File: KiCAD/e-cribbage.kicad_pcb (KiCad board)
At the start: 2 copper layers, 304.8 x 100.3 mm, 569 parts, among them J1 Conn_01x04_Female, U1 74HC595D_118, U10 74HC595D_118, U11 74HC595D_118, U12 74HC595D_118, U13 74HC595D_118, U14 74HC595D_118, U15 74HC595D_118, U16 74HC595D_118, U17 74HC595D_118, U18 74HC595D_118, U19 74HC595D_118, U2 MSP430F2012IPW, U20 74HC595D_118, U21 74HC595D_118, U22 74HC595D_118, U23 74HC595D_118, U24 74HC595D_118, U25 74HC595D_118, U26 74HC595D_118, U27 74HC595D_118, U28 74HC595D_118, U29 74HC595D_118, U3 74HC595D_118, U30 74HC595D_118, U31 74HC595D_118, U32 SN74LVC1G08DBVR, U34 SN74LVC1G08DBVR, U35 SN74LVC1G08DBVR, U36 SN74LVC1G08DBVR, U37 SN74LVC1G08DBVR, U38 SN74LVC1G08DBVR, U39 SN74LVC1G08DBVR, U4 74HC595D_118, U40 SN74LVC1G08DBVR, U5 74HC595D_118, U6 74HC595D_118, U7 74HC595D_118, U8 74HC595D_118, U9 74HC595D_118

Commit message: initial routing complete
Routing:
- net CLK2B: track 114.2 -> 430.7 mm, vias 4 -> 8
- net CLK1B: track 281.6 -> 478.3 mm, vias 1 -> 5
- net Net-(U13-Pad9): track 0.00 -> 143.7 mm, vias 0 -> 6
- net CLK1C: track 44.0 -> 176.4 mm, vias 2 -> 4
- net CLK2C: track 244.9 -> 375.6 mm, vias 2 -> 5
- net CLK2A: track 325.9 -> 436.0 mm, vias 4 -> 7
- net Net-(U11-Pad9): track 0.00 -> 102.4 mm, vias 0 -> 2
- net Net-(U27-Pad9): track 0.00 -> 90.5 mm, vias 0 -> 2
- net Net-(U22-Pad9): track 0.00 -> 73.7 mm, vias 0 -> 2
- net Net-(U10-Pad14): track 0.00 -> 69.2 mm, vias 0 -> 2
- net Net-(U8-Pad9): track 0.00 -> 66.4 mm, vias 0 -> 2
- net Net-(U24-Pad9): track 0.00 -> 65.6 mm, vias 0 -> 2
- net Net-(U10-Pad9): track 0.00 -> 46.1 mm, vias 0 -> 4
- net Net-(U6-Pad9): track 0.00 -> 42.8 mm, vias 0 -> 3
- net Net-(U28-Pad9): track 0.00 -> 42.2 mm, vias 0 -> 2
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
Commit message: Layout - routed switch, usb, linear reg
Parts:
- added J2: USB_B_Micro, Connector_USB:USB_Micro-B_Molex_47346-0001, F.Cu at (58.5, 177.8)
- added S5: EG1218, digikey-footprints:Switch_Slide_11.6x4mm_EG1218, F.Cu at (73.5, 174.8)
- added U33: TPS22929D, Package_TO_SOT_SMD:SOT-23-6, F.Cu at (73.3, 168.8)
- added U41: LM317T, digikey-footprints:TO-220-3, F.Cu at (67.2, 168.1)
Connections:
- BAT1 pad 1: +3V3 -> +BATT
- C2 pad 1: +3V3 -> VS
- J1 pad 1: +3V3 -> VS
- R243 pad 2: +3V3 -> VS
- R244 pad 2: +3V3 -> VS
- R246 pad 2: +3V3 -> VS
- R247 pad 2: +3V3 -> VS
- R251 pad 2: +3V3 -> VS
- U16 pad 9: (no net) -> Net-(U16-Pad9)
- U2 pad 1: +3V3 -> VS
- U2 pad 6: (no net) -> Net-(U2-Pad6)
- U2 pad 9: (no net) -> Net-(U2-Pad9)
- U23 pad 9: (no net) -> Net-(U23-Pad9)
- U24 pad 14: (no net) -> Net-(U24-Pad14)
- U31 pad 9: (no net) -> Net-(U31-Pad9)
- U7 pad 9: (no net) -> Net-(U7-Pad9)
- U8 pad 14: (no net) -> Net-(U8-Pad14)
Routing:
- net VS: track 0.00 -> 132.3 mm, vias 0 -> 8
- net Net-(U2-Pad9): track 0.00 -> 91.0 mm, vias 0 -> 4
- net GND: track 949.0 -> 1034.0 mm, vias 335 -> 336
- net +BATT: track 0.00 -> 31.3 mm
- net +3V3: track 498.9 -> 483.5 mm, vias 90 -> 88
- net Net-(J2-Pad1): track 0.00 -> 10.4 mm, vias 0 -> 1
- net Net-(S5-Pad3): track 0.00 -> 9.19 mm
- net DATA: track 202.4 -> 208.1 mm
- net Net-(C33-Pad1): track 212.3 -> 208.1 mm
- net Net-(C32-Pad1): track 187.8 -> 183.9 mm
- net Net-(C35-Pad1): track 188.6 -> 185.0 mm
- net Net-(C34-Pad1): track 173.3 -> 170.2 mm
- net LE1: track 74.3 -> 75.4 mm

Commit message: Layout: routed USB power and switch, silkscreen
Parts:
- added C40: 1.0uF, Capacitor_SMD:C_0603_1608Metric_Pad1.05x0.95mm_HandSolder, F.Cu at (89.2, 171.7)
- added C41: 1.0uF, Capacitor_SMD:C_0603_1608Metric_Pad1.05x0.95mm_HandSolder, F.Cu at (81.7, 171.3)
- added C42: 1.0uF, Capacitor_SMD:C_0603_1608Metric_Pad1.05x0.95mm_HandSolder, F.Cu at (55.6, 171.1)
- added C43: 1.0uF, Capacitor_SMD:C_0603_1608Metric_Pad1.05x0.95mm_HandSolder, F.Cu at (64.1, 172.3)
- C4: footprint Capacitors_SMD:C_0603_HandSoldering -> Capacitor_SMD:C_0603_1608Metric_Pad1.05x0.95mm_HandSolder
- S5: footprint digikey-footprints:Switch_Slide_11.6x4mm_EG1218 -> Button_Switch_SMD:SW_SPDT_CK-JS102011SAQN
- U41: value LM317T -> TLV71333PDBV; footprint digikey-footprints:TO-220-3 -> Package_TO_SOT_SMD:SOT-23-5
- moved U33 12.8 mm to (85.9, 171.4)
- moved U41 6.94 mm to (60.8, 170.9), turned to 0 degrees
- moved S5 3.70 mm to (70.5, 176.9), turned to 0 degrees
- moved C18 0.89 mm to (206.3, 90.2)
- moved J2 0.51 mm to (58.5, 177.3)
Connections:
- J2 pad 1: Net-(J2-Pad1) -> Net-(C42-Pad1)
- S5 pad 1: +BATT -> Net-(C43-Pad1)
- S5 pad 3: Net-(S5-Pad3) -> +BATT
- U1 pad 12: CLK1A -> RCLK
- U10 pad 12: CLK1C -> RCLK
- U11 pad 12: CLK1C -> RCLK
- U12 pad 12: CLK1C -> RCLK
- U13 pad 12: CLK1C -> RCLK
- U14 pad 12: CLK1D -> RCLK
- U15 pad 12: CLK1D -> RCLK
- U16 pad 12: CLK1D -> RCLK
- U17 pad 12: CLK2A -> RCLK
- U18 pad 12: CLK2A -> RCLK
- U19 pad 12: CLK2A -> RCLK
- U2 pad 6: Net-(U2-Pad6) -> RCLK
- U20 pad 12: CLK2A -> RCLK
- U21 pad 12: CLK2B -> RCLK
- U22 pad 12: CLK2B -> RCLK
- U23 pad 12: CLK2B -> RCLK
- U24 pad 12: CLK2B -> RCLK
- U25 pad 12: CLK2C -> RCLK
- U26 pad 12: CLK2C -> RCLK
- U27 pad 12: CLK2C -> RCLK
- U28 pad 12: CLK2C -> RCLK
- U29 pad 12: CLK2D -> RCLK
- U3 pad 12: CLK1A -> RCLK
- U30 pad 12: CLK2D -> RCLK
- U31 pad 12: CLK2D -> RCLK
- U4 pad 12: CLK1A -> RCLK
- U41 pad 1: GND -> Net-(C42-Pad1)
- U41 pad 2: Net-(S5-Pad3) -> GND
- U41 pad 3: Net-(J2-Pad1) -> Net-(C42-Pad1)
- U5 pad 12: CLK1A -> RCLK
- U6 pad 12: CLK1B -> RCLK
- U7 pad 12: CLK1B -> RCLK
- U8 pad 12: CLK1B -> RCLK
- U8 pad 14: Net-(U8-Pad14) -> Net-(U7-Pad9)
- U9 pad 12: CLK1B -> RCLK
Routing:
- net RCLK: track 0.00 -> 768.1 mm, vias 0 -> 12
- net CLK2A: track 436.0 -> 325.4 mm, vias 7 -> 4
- net CLK1A: track 378.9 -> 314.4 mm, vias 6 -> 5
- net GND: track 1034.0 -> 1002.9 mm, vias 336 -> 349
- net +3V3: track 483.5 -> 464.1 mm, vias 88 -> 90
- net Net-(C42-Pad1): track 0.00 -> 14.0 mm
- net Net-(C43-Pad1): track 0.00 -> 10.7 mm
- net Net-(J2-Pad1): track 10.4 -> 0.00 mm, vias 1 -> 0
- net CLK1B: track 478.3 -> 468.5 mm, vias 5 -> 4
- net Net-(S5-Pad3): track 9.19 -> 0.00 mm
- net Net-(C34-Pad1): track 170.2 -> 163.2 mm
- net Net-(C33-Pad1): track 208.1 -> 201.2 mm
- net Net-(C32-Pad1): track 183.9 -> 177.0 mm
- net Net-(C35-Pad1): track 185.0 -> 178.1 mm
- net Net-(U2-Pad9): track 91.0 -> 85.3 mm, vias 4 -> 6
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
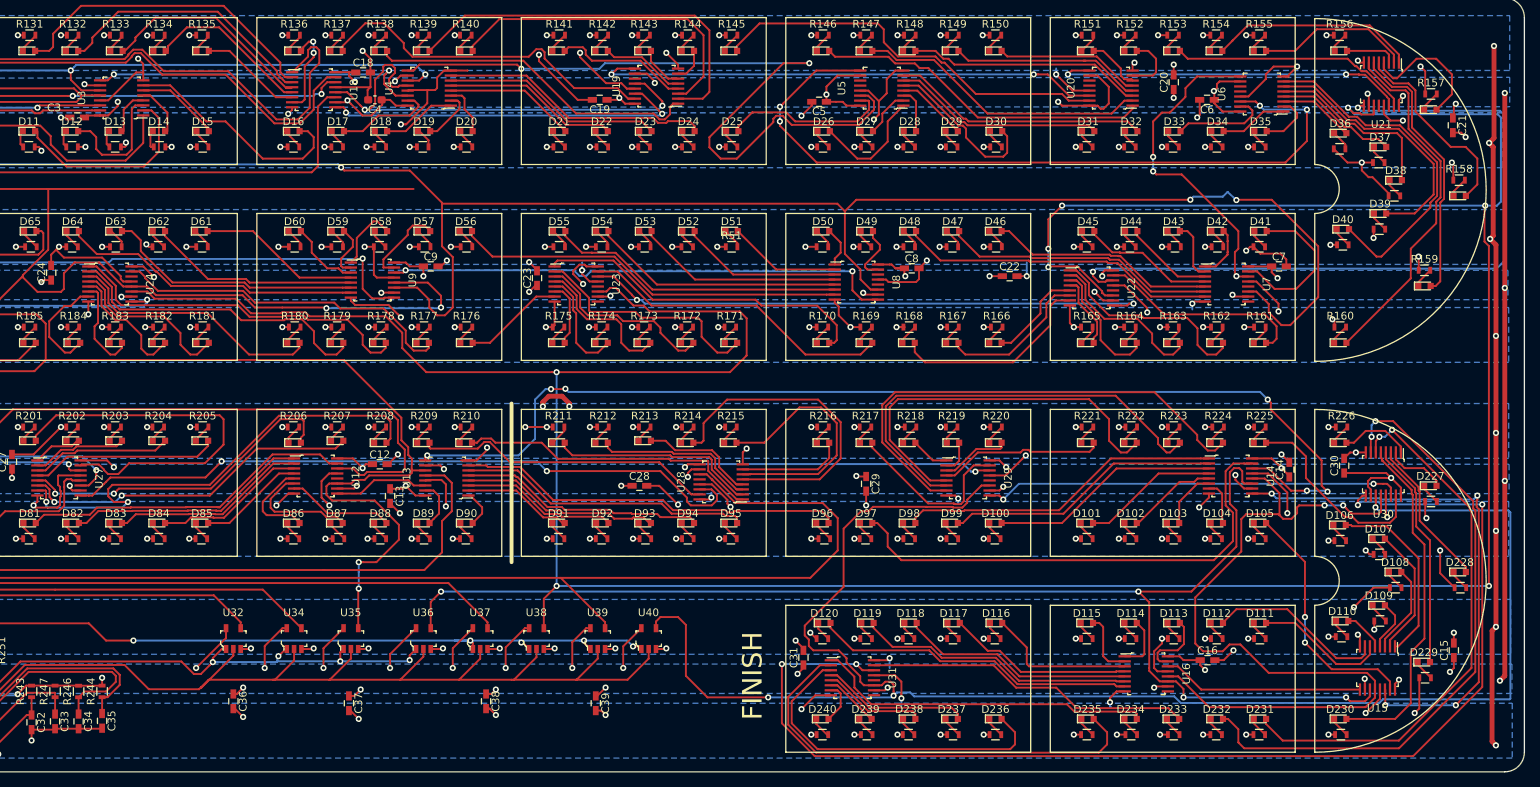
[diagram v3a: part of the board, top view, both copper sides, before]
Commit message: Finished RCLK routes
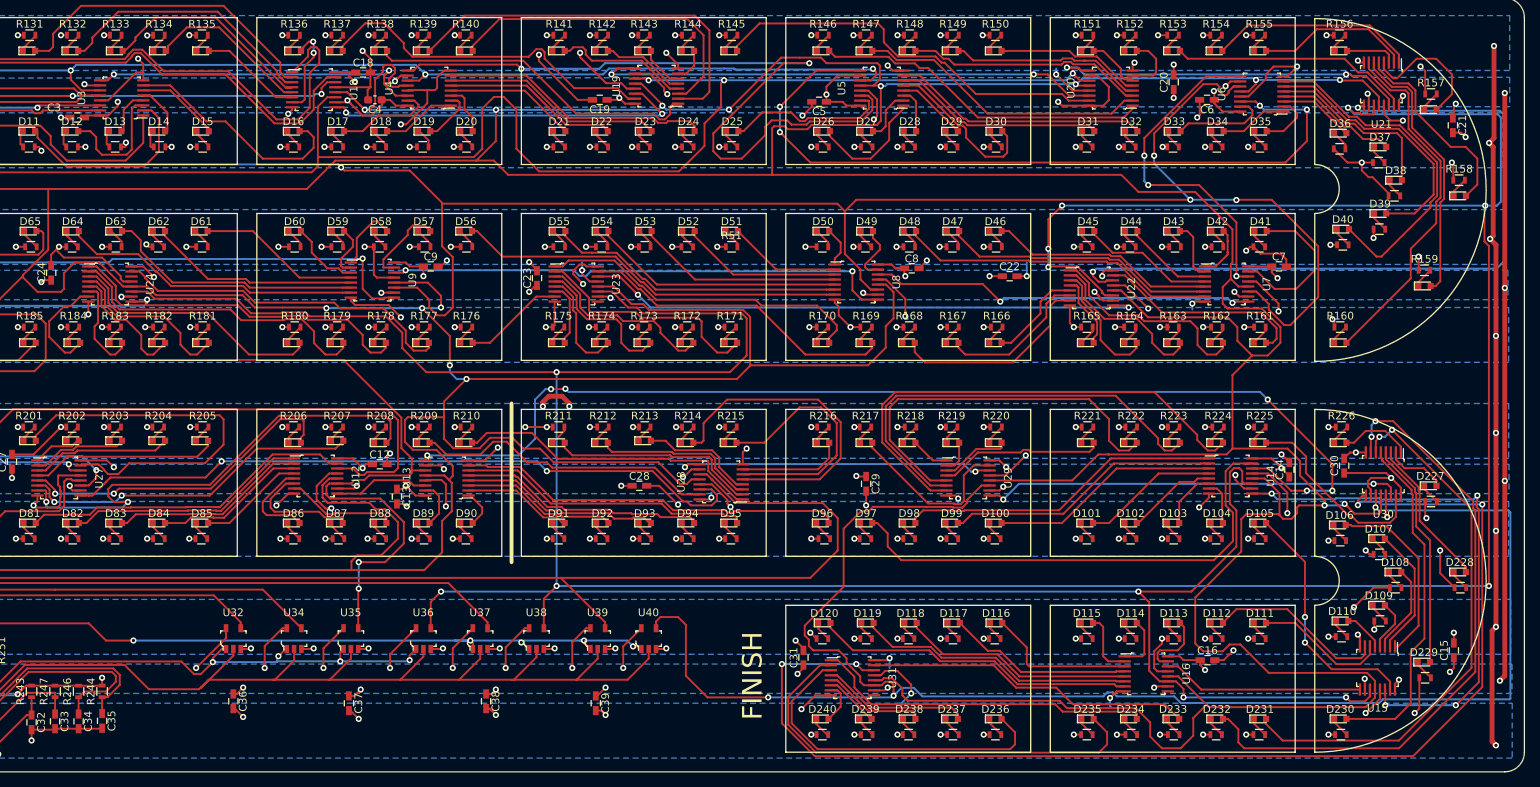
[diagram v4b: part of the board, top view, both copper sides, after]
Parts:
- moved C13 0.89 mm to (210.7, 145.2)
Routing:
- net RCLK: track 768.1 -> 1382.7 mm, vias 12 -> 21
- net CLK2A: track 325.4 -> 459.5 mm, vias 4 -> 7
- net CLK1A: track 314.4 -> 376.1 mm, vias 5 -> 6
- net Net-(U7-Pad9): track 0.00 -> 50.0 mm, vias 0 -> 2
- net CLK1B: track 468.5 -> 493.4 mm, vias 4 -> 5
- net CLK1C: track 175.3 -> 177.1 mm
- net GND: track 1002.9 -> 1001.2 mm, vias 349 -> 351
- net Net-(U11-Pad9): track 102.4 -> 101.1 mm
- net Net-(U6-Pad9): track 42.8 -> 44.0 mm
- net Net-(U22-Pad9): track 73.7 -> 72.6 mm
- net CLK2D: track 218.9 -> 219.8 mm
- net +3V3: track 464.1 -> 463.2 mm, vias 90 -> 91
- net Net-(U4-Pad9): track 100.1 -> 99.3 mm
- net Net-(U13-Pad9): track 143.7 -> 144.4 mm
- net Net-(D170-Pad2): track 43.7 -> 43.1 mm
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
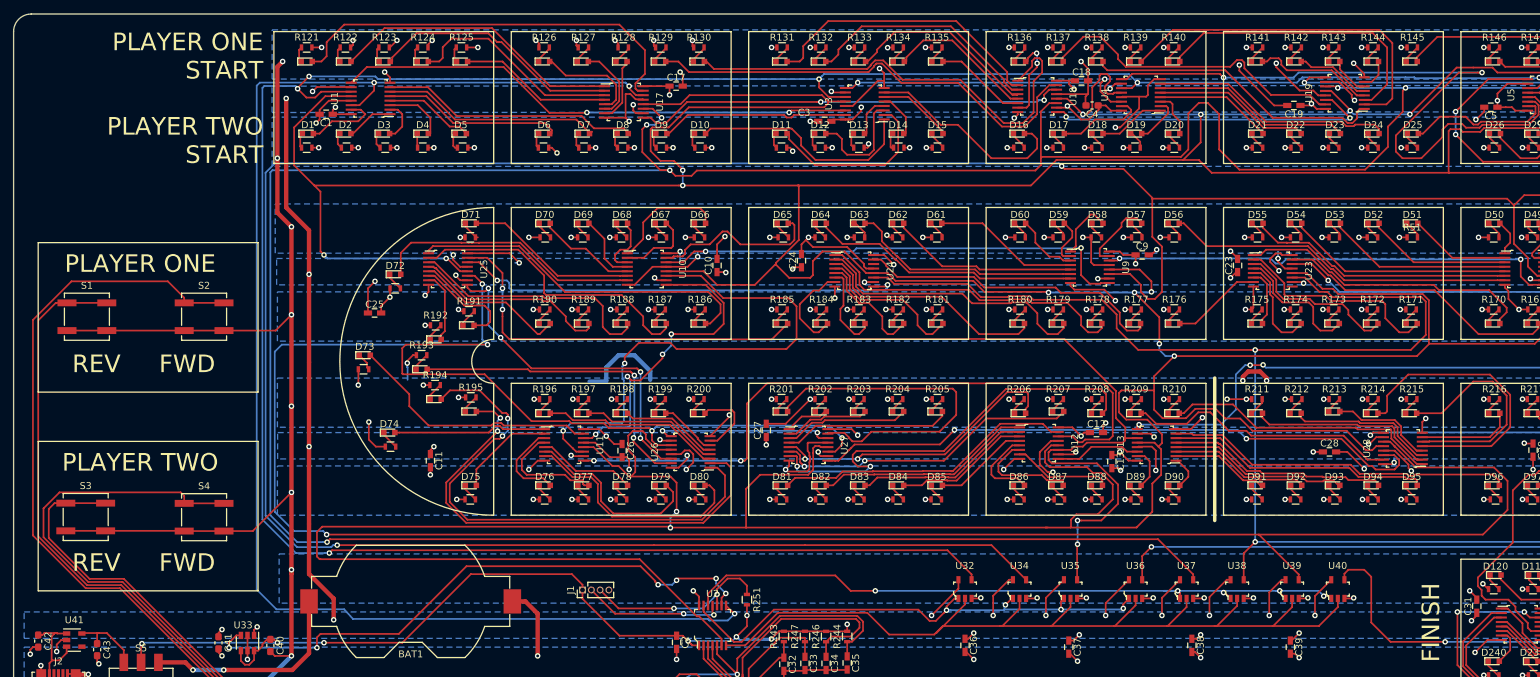
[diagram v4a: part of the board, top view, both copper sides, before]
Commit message: fixed broken connection on U24-14
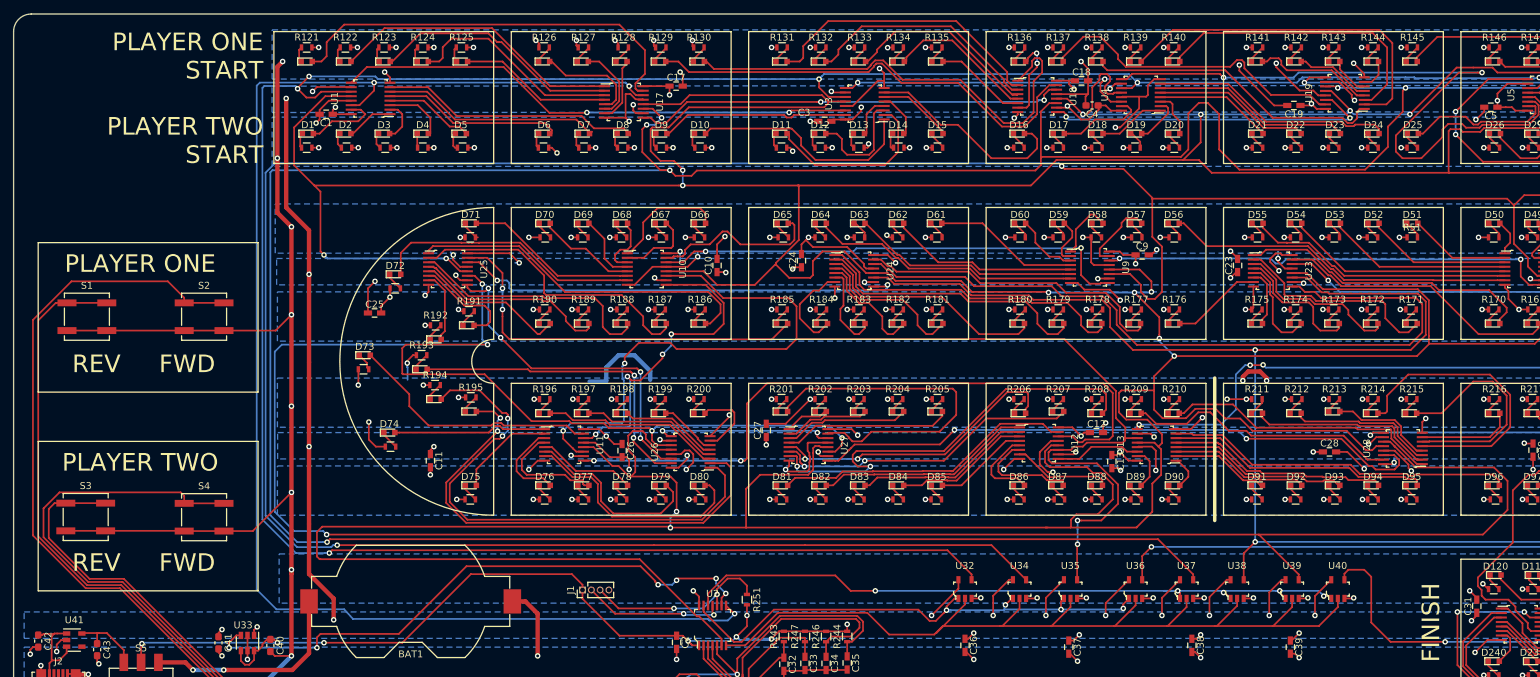
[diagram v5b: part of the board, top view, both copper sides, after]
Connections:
- U24 pad 14: Net-(U24-Pad14) -> Net-(U23-Pad9)
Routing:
- net Net-(U23-Pad9): track 0.00 -> 110.0 mm
- net GND: track 1001.2 -> 998.7 mm
- net Net-(D63-Pad2): track 33.5 -> 32.7 mm
- net RCLK: track 1382.7 -> 1381.9 mm

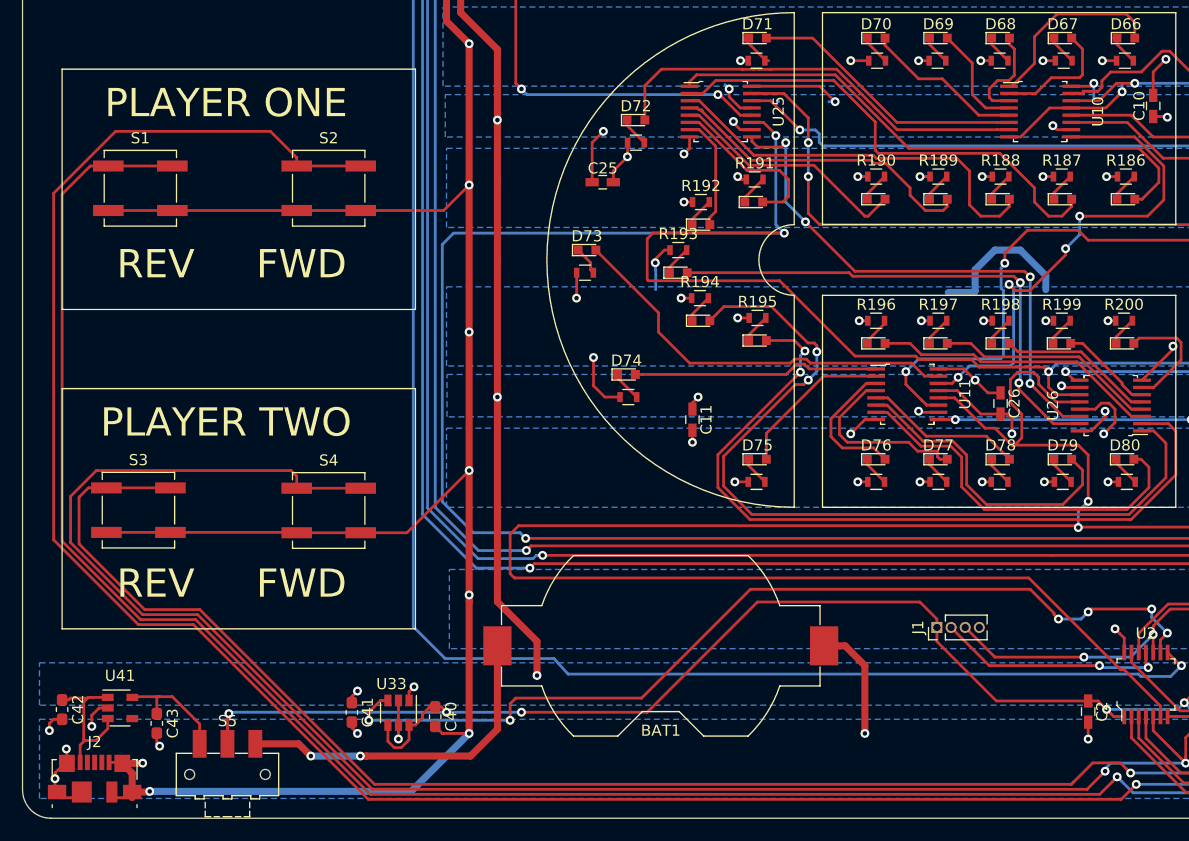
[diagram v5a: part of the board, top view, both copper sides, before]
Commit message: replaced S1 with TH push button
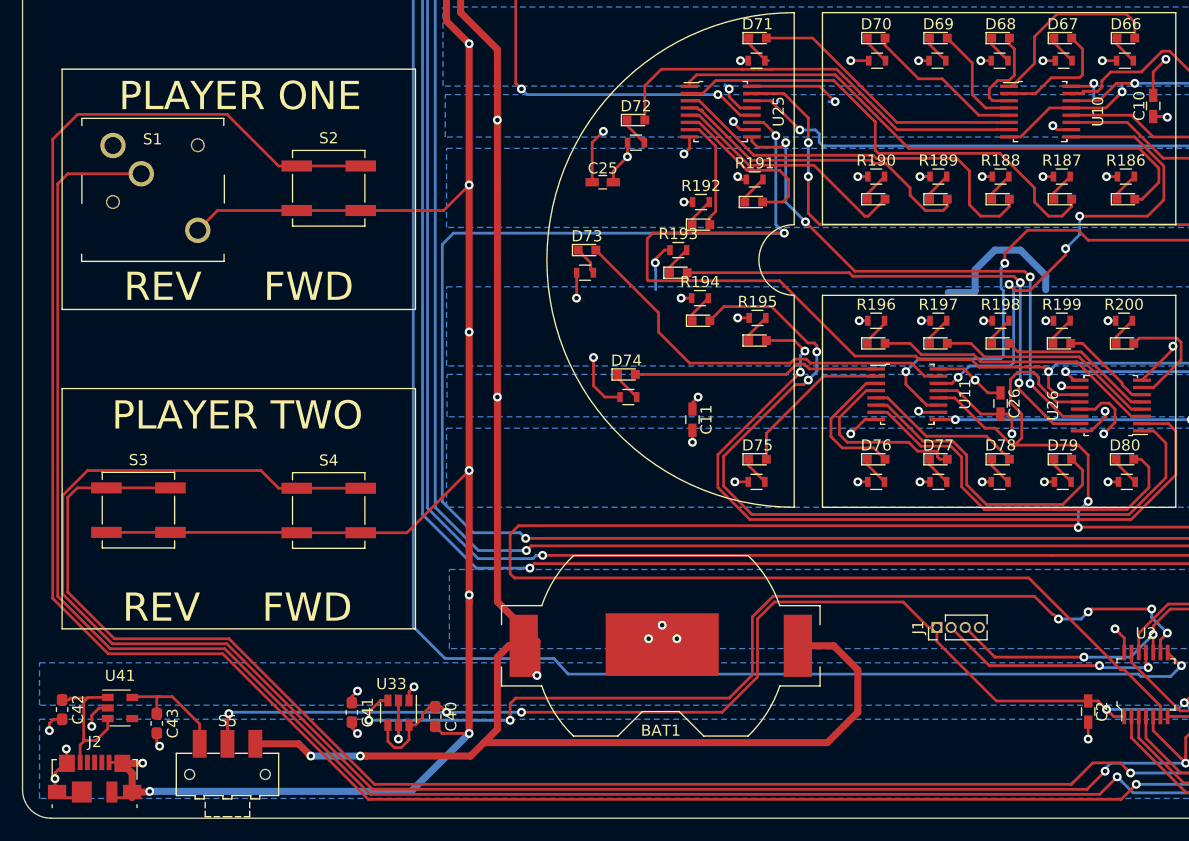
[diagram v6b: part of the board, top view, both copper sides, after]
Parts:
- BAT1: value BS-7 -> BC-2003-G
- S1: value GPTS203211B -> KS11R22; footprint Buttons_Switches_SMD:SW_SPST_B3SL-1002P -> e-cribbage:KS11R22
- S2, S3, S4: value GPTS203211B -> KS11R22
- moved S1 1.10 mm to (63.8, 124.3)
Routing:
- net +BATT: track 30.7 -> 155.4 mm, vias 2 -> 6
- net +3V3: track 463.4 -> 385.2 mm, vias 91 -> 87
- net GND: track 998.7 -> 985.6 mm, vias 351 -> 353
- net Net-(C33-Pad1): track 201.2 -> 208.1 mm
- net Net-(C34-Pad1): track 163.2 -> 167.8 mm
- net Net-(C35-Pad1): track 178.1 -> 181.6 mm
- net VS: track 133.4 -> 136.0 mm
- net Net-(U2-Pad9): track 85.3 -> 87.7 mm
- net Net-(C32-Pad1): track 177.0 -> 178.1 mm

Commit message: library and layout cleanup
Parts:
- BAT1: value BC-2003-G -> BS-7
- C1, C10, C11, C12, C13, C14, C15, C16, C17, C18, C19, C2, C20, C21, C22, C23, C24, C25, C26, C27, C28, C29, C3, C30, C31, C32, C33, C34, C35, C36, C37, C38, C39, C5, C6, C7, C8, C9: value 1.0uF -> 0.1uF; footprint Capacitors_SMD:C_0603_HandSoldering -> e-cribbage:C_0603_1608Metric_Pad1.05x0.95mm_HandSolder
- C4: value 1.0uF -> 0.1uF
- D1, D10, D100, D101, D102, D103, D104, D105, D106, D107, D108, D109, D11, D110, D111, D112, D113, D114, D115, D116, D117, D118, D119, D12, D120, D13, D14, D15, D16, D17, D18, D19, D2, D20, D21, D22, D23, D24, D25, D26, D27, D28, D29, D3, D30, D31, D32, D33, D34, D35, D36, D37, D38, D39, D4, D40, D41, D42, D43, D44, D45, D46, D47, D48, D49, D5, D50, D51, D52, D53, D54, D55, D56, D57, D58, D59, D6, D60, D61, D62, D63, D64, D65, D66, D67, D68, D69, D7, D70, D71, D72, D73, D74, D75, D76, D77, D78, D79, D8, D80, D81, D82, D83, D84, D85, D86, D87, D88, D89, D9, D90, D91, D92, D93, D94, D95, D96, D97, D98, D99: value LED -> LED1
- D121, D122, D123, D124, D125, D126, D127, D128, D129, D130, D131, D132, D133, D134, D135, D136, D137, D138, D139, D140, D141, D142, D143, D144, D145, D146, D147, D148, D149, D150, D151, D152, D153, D154, D155, D156, D157, D158, D159, D160, D161, D162, D163, D164, D165, D166, D167, D168, D169, D170, D171, D172, D173, D174, D175, D176, D177, D178, D179, D180, D181, D182, D183, D184, D185, D186, D187, D188, D189, D190, D191, D192, D193, D194, D195, D196, D197, D198, D199, D200, D201, D202, D203, D204, D205, D206, D207, D208, D209, D210, D211, D212, D213, D214, D215, D216, D217, D218, D219, D220, D221, D222, D223, D224, D225, D226, D227, D228, D229, D230, D231, D232, D233, D234, D235, D236, D237, D238, D239, D240: value LED -> LED2
- S1: value KS11R22 -> GPTS203211B; footprint e-cribbage:KS11R22 -> w_switch:KS12R22
- S2, S3, S4: value KS11R22 -> GPTS203211B; footprint Buttons_Switches_SMD:SW_SPST_B3SL-1002P -> w_switch:KS12R22
- U1, U10, U11, U12, U13, U14, U15, U16, U17, U18, U19, U20, U21, U22, U23, U24, U25, U26, U27, U28, U29, U3, U30, U31, U4, U5, U6, U7, U8, U9: footprint digikey-footprints:TSSOP-16_W4.40mm -> e-cribbage:TSSOP-16_W4.40mm
- U2: footprint digikey-footprints:TSSOP-14_W4.4mm -> e-cribbage:TSSOP-14_W4.4mm
- moved C3 6.20 mm to (165.5, 91.1)
- moved S2 0.47 mm to (79.1, 124.3)
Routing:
- net +BATT: track 155.4 -> 76.5 mm, vias 6 -> 2
- net +3V3: track 385.2 -> 463.0 mm, vias 87 -> 92
- net Net-(C32-Pad1): track 178.1 -> 183.9 mm
- net Net-(C35-Pad1): track 181.6 -> 184.9 mm
- net GND: track 985.6 -> 988.6 mm
- net Net-(C34-Pad1): track 167.8 -> 169.5 mm
- net Net-(D191-Pad2): track 15.1 -> 14.0 mm
- net Net-(D40-Pad2): track 45.1 -> 44.1 mm
- net CLK2C: track 372.6 -> 371.6 mm
- net Net-(C33-Pad1): track 208.1 -> 207.2 mm
- net CLK1A: track 376.1 -> 376.7 mm
